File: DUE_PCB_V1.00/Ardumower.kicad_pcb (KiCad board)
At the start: 2 copper layers, 169.8 x 97 mm, 86 parts, among them J1 9V IN, J10 Sonar_R, J11 Sonar_C, J12 Sonar_L, J13 P_Right, J14 Buzzer, J15 Button, J16 US1, J17 US2, J18 US3, J19 P_Left, J2 I2C0_1, J20 Remote, J21 PCB_2, J22 Ser0, J23 Ser1, J24 Ser2, J25 5V IN, J26 Cutter1, J27 MotorR, J28 MotorL, J29 3.3V IN, J3 I2C0_2, J30 I2C1_2, J31 Ser3, J32 24V In, J33 ReserveD8, J34 ReserveD9, J35 ReserveD49, J36 ReserveA10, J37 RPM_Mow, J38 ODO_Left, J39 ODO_Right, J4 I2C1_1, J40 Motor_Right, J41 Motor_Left, J42 Cutter, J5 Bumper, J6 Drop_Left, J7 Drop_Right, J8 Tilt, J9 Rain, U1 MC33926, U2 MC33926

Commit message: First Route Test
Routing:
- net GND: track 0.00 -> 656.8 mm
- net +3V3: track 0.00 -> 336.2 mm
- net +5V: track 0.00 -> 323.6 mm, vias 0 -> 1
- net IOREV: track 0.00 -> 163.4 mm
- net pinBuzzer: track 0.00 -> 129.3 mm
- net pinChargeRelay: track 0.00 -> 128.2 mm
- net pinRemoteSwitch: track 0.00 -> 126.1 mm
- net pinButton: track 0.00 -> 125.1 mm
- net pinUserSwitch3: track 0.00 -> 121.3 mm
- net pinMotorMowSense: track 0.00 -> 117.9 mm, vias 0 -> 1
- net pinMotorLeftPWM: track 0.00 -> 116.1 mm
- net pinDropRight: track 0.00 -> 109.7 mm
- net pinChargeVoltage: track 0.00 -> 106.5 mm, vias 0 -> 1
- net pinMotorRightPWM: track 0.00 -> 104.5 mm
- net pinChargeCurrent: track 0.00 -> 102.8 mm, vias 0 -> 1
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
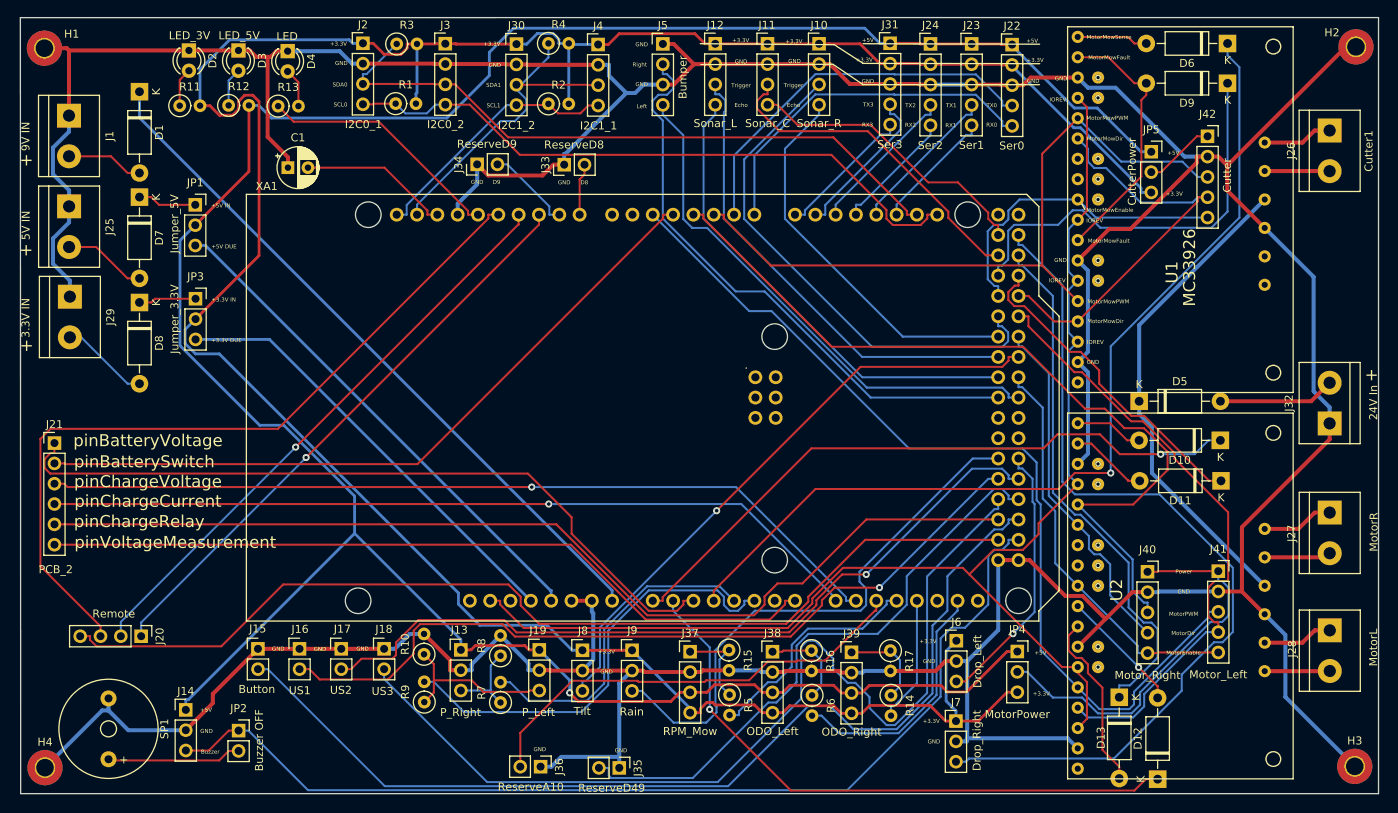
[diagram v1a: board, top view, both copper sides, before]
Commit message: Small changes in Line Traces
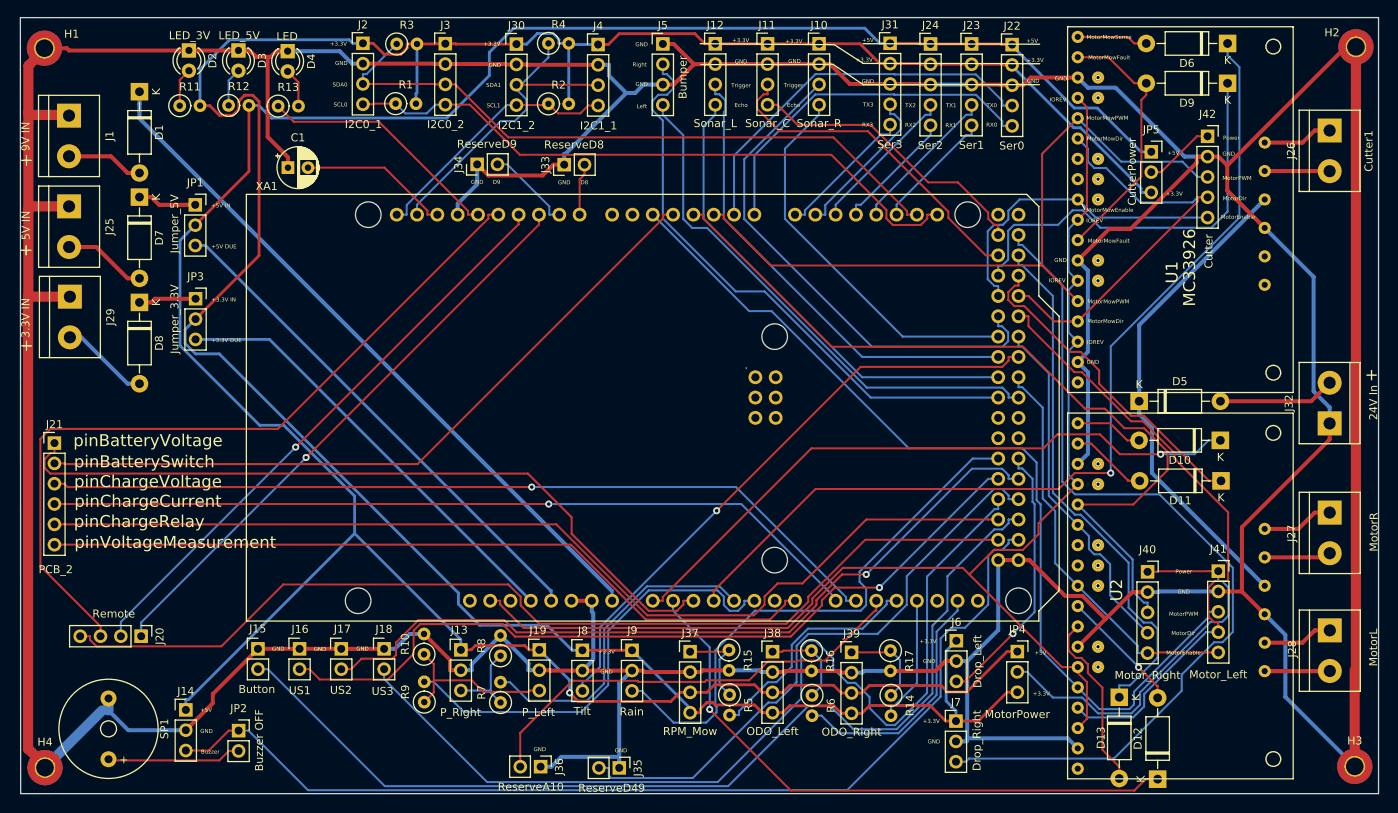
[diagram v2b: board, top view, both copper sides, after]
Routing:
- net GND: track 656.8 -> 822.6 mm

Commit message: Add Gerber Files
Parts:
- added REF**: WEEE-Logo_4.2x6mm_SilkScreen, Symbol:WEEE-Logo_4.2x6mm_SilkScreen, F.Cu at (84.9, 127.2)
- added REF**: ESD-Logo_8.9x8mm_SilkScreen, Symbol:ESD-Logo_8.9x8mm_SilkScreen, F.Cu at (75.8, 125.8)
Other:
- board text added: "Simple Mower Main PCB v1.01 by SD 05/2021 Attention only for Arduino DUE"

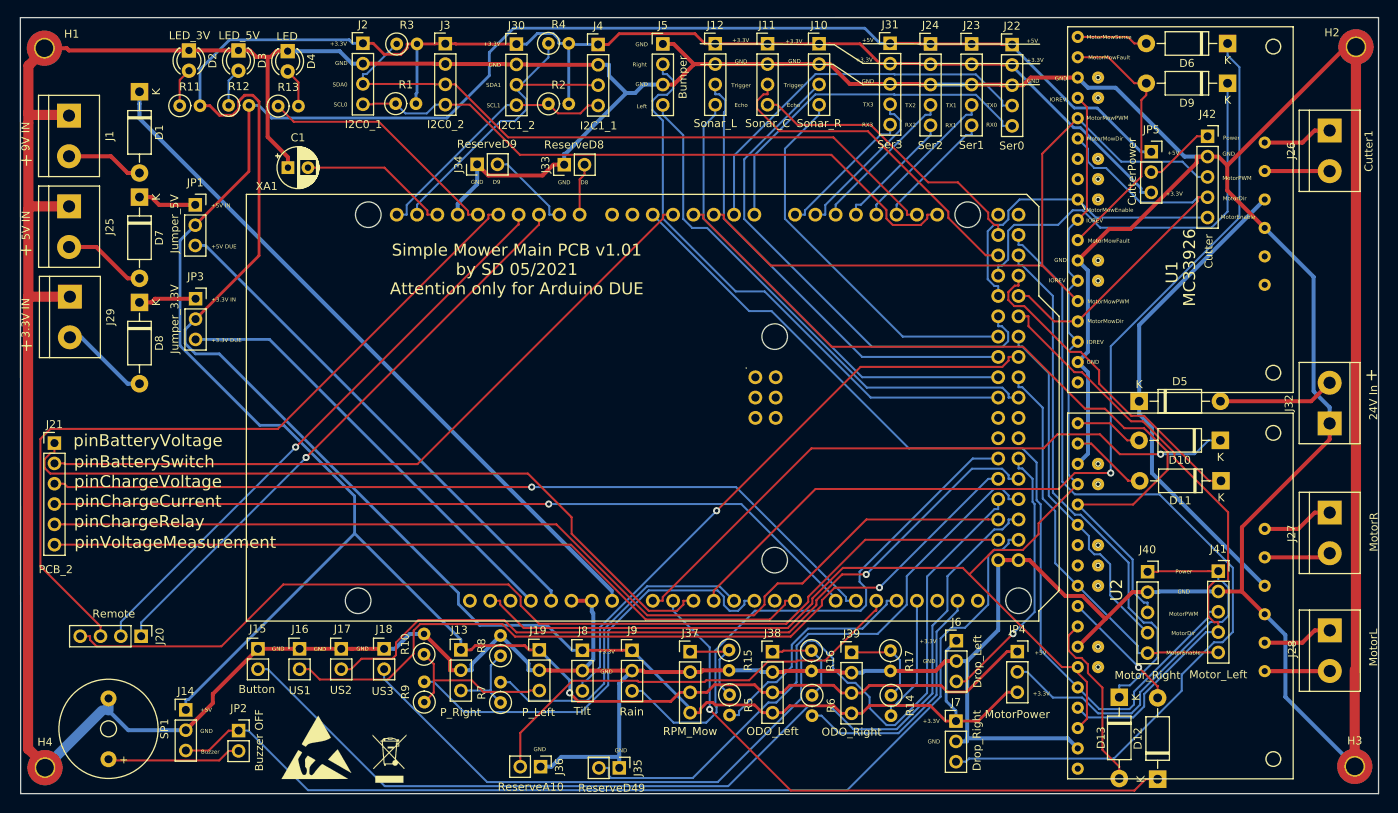
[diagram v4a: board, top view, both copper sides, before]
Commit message: Remove 24V from PCB
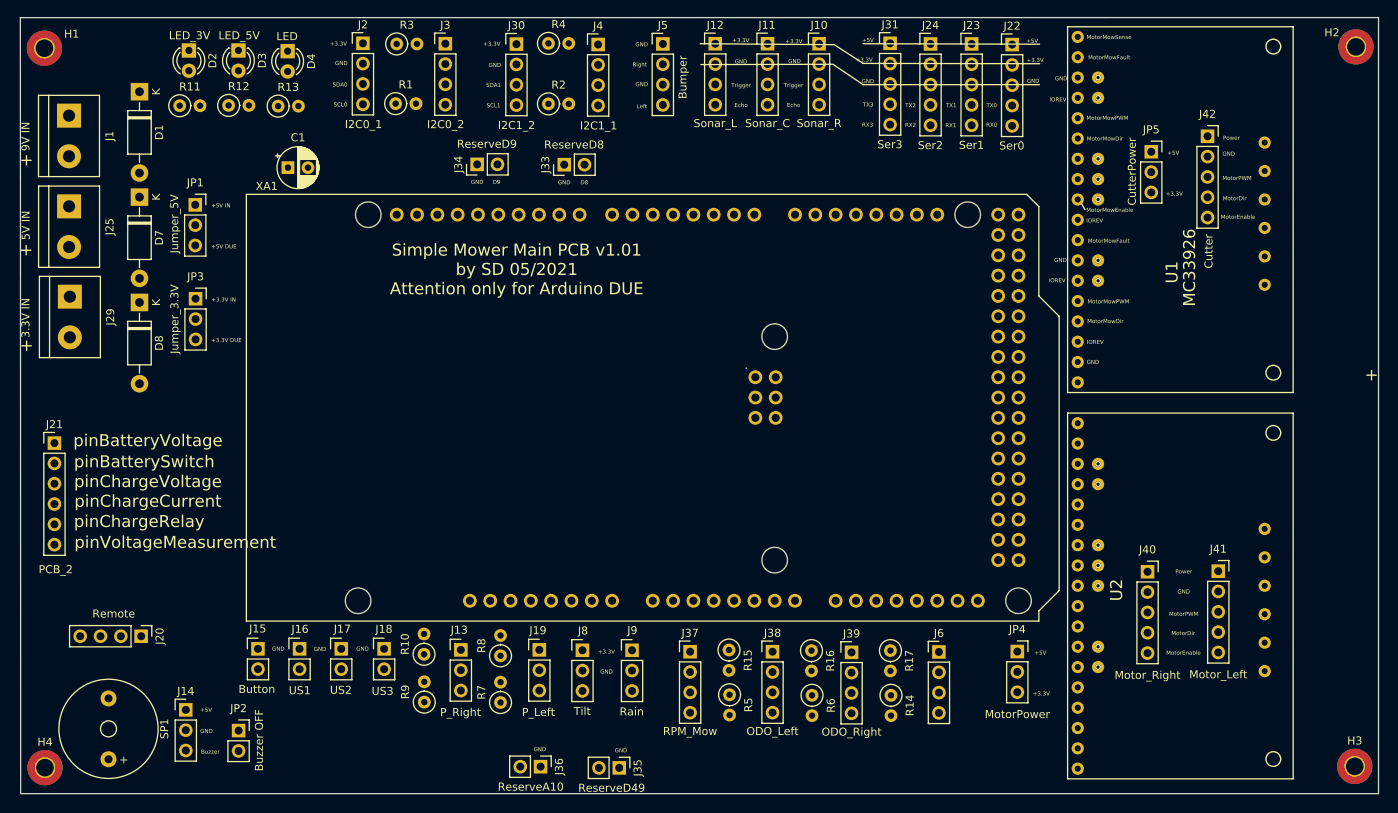
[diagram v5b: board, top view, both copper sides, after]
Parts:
- removed D10, D11, D12, D13, D5, D6, D9: 1N4728A, Diode_THT:D_DO-41_SOD81_P10.16mm_Horizontal
- removed J26: Cutter1, TerminalBlock:TerminalBlock_bornier-2_P5.08mm
- removed J27: MotorR, TerminalBlock:TerminalBlock_bornier-2_P5.08mm
- removed J28: MotorL, TerminalBlock:TerminalBlock_bornier-2_P5.08mm
- removed J32: 24V In, TerminalBlock:TerminalBlock_bornier-2_P5.08mm
- removed J7: Drop_Right, Connector_PinHeader_2.54mm:PinHeader_1x03_P2.54mm_Vertical
- removed REF**: WEEE-Logo_4.2x6mm_SilkScreen, Symbol:WEEE-Logo_4.2x6mm_SilkScreen
- removed REF**: ESD-Logo_8.9x8mm_SilkScreen, Symbol:ESD-Logo_8.9x8mm_SilkScreen
- J6: value Drop_Left -> Drop; footprint Connector_PinHeader_2.54mm:PinHeader_1x03_P2.54mm_Vertical -> Connector_PinHeader_2.54mm:PinHeader_1x04_P2.54mm_Vertical
- moved J6 2.59 mm to (153.6, 113.9)
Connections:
- J21 pad 6: pinVoltageMeasurement -> +3V3
- J6 pad 1: +3V3 -> GND
- J6 pad 2: GND -> pinDropLeft
- J6 pad 3: pinDropLeft -> GND
- U1 pad 17: Net-(D9-Pad2) -> pinMotorMowFault
- U1 pad 18: Net-(D6-Pad2) -> pinMotorMowSense
- U1 pad 21: GND -> (no net)
- U1 pad 22: +24V -> (no net)
- U1 pad 23: Net-(J26-Pad2) -> (no net)
- U1 pad 24: Net-(J26-Pad1) -> (no net)
- U1 pad 8: Net-(D9-Pad2) -> pinMotorMowFault
- U2 pad 17: Net-(D11-Pad2) -> pinMotorRightFault
- U2 pad 18: Net-(D10-Pad2) -> pinMotorRightSense
- U2 pad 19: Net-(J28-Pad2) -> (no net)
- U2 pad 20: Net-(J28-Pad1) -> (no net)
- U2 pad 21: GND -> (no net)
- U2 pad 22: +24V -> (no net)
- U2 pad 23: Net-(J27-Pad2) -> (no net)
- U2 pad 24: Net-(J27-Pad1) -> (no net)
- U2 pad 8: Net-(D13-Pad2) -> pinMotorLeftFault
- U2 pad 9: Net-(D12-Pad2) -> pinMotorLeftSense
- XA1 pad A7: pinVoltageMeasurement -> (no net)
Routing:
- net GND: track 822.6 -> 0.00 mm
- net +3V3: track 336.2 -> 0.00 mm
- net +5V: track 323.6 -> 0.00 mm, vias 1 -> 0
- net IOREV: track 163.4 -> 0.00 mm
- net pinBuzzer: track 129.3 -> 0.00 mm
- net pinChargeRelay: track 128.2 -> 0.00 mm
- net pinRemoteSwitch: track 126.1 -> 0.00 mm
- net pinButton: track 125.1 -> 0.00 mm
- net pinUserSwitch3: track 121.3 -> 0.00 mm
- net pinMotorMowSense: track 117.9 -> 0.00 mm, vias 1 -> 0
- net pinMotorLeftPWM: track 116.1 -> 0.00 mm
- net pinDropRight: track 109.7 -> 0.00 mm
- net pinChargeVoltage: track 106.5 -> 0.00 mm, vias 1 -> 0
- net pinMotorRightPWM: track 104.5 -> 0.00 mm
- net pinChargeCurrent: track 102.8 -> 0.00 mm, vias 1 -> 0
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
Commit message: Add 2 new Motor Connectors and Odo
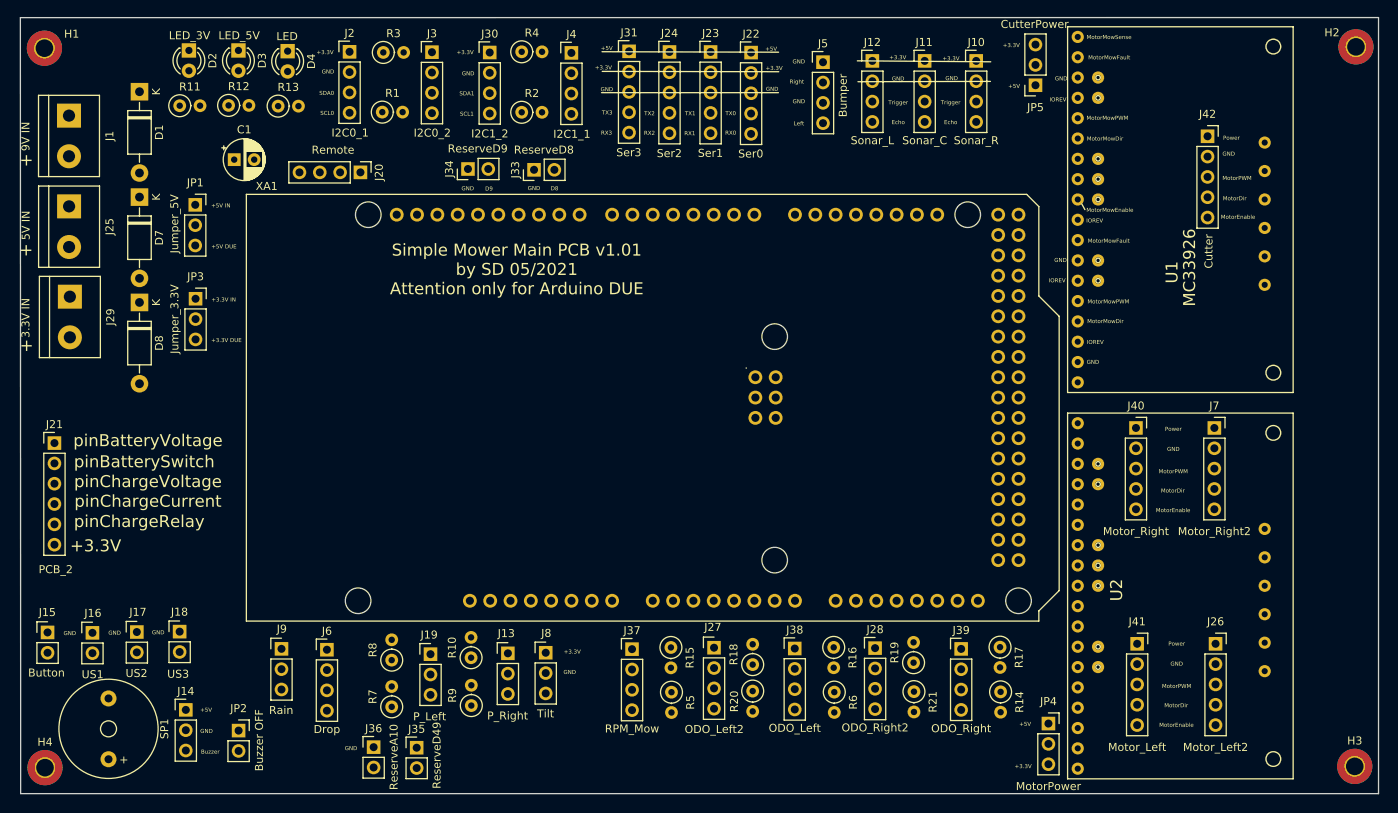
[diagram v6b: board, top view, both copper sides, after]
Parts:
- added J26: Motor_Left2, Connector_PinSocket_2.54mm:PinSocket_1x05_P2.54mm_Vertical, F.Cu at (188.2, 112.9)
- added J27: ODO_Left2, Connector_PinHeader_2.54mm:PinHeader_1x04_P2.54mm_Vertical, F.Cu at (125.5, 113.4)
- added J28: ODO_Right2, Connector_PinHeader_2.54mm:PinHeader_1x04_P2.54mm_Vertical, F.Cu at (145.6, 113.4)
- added J7: Motor_Right2, Connector_PinSocket_2.54mm:PinSocket_1x05_P2.54mm_Vertical, F.Cu at (188.1, 85.9)
- added R18: 1KO, Resistor_THT:R_Axial_DIN0207_L6.3mm_D2.5mm_P2.54mm_Vertical, F.Cu at (130.3, 115.5)
- added R19: 1KO, Resistor_THT:R_Axial_DIN0207_L6.3mm_D2.5mm_P2.54mm_Vertical, F.Cu at (150.4, 115.2)
- added R20: 1,5KO, Resistor_THT:R_Axial_DIN0207_L6.3mm_D2.5mm_P2.54mm_Vertical, F.Cu at (130.3, 118.8)
- added R21: 1,5KO, Resistor_THT:R_Axial_DIN0207_L6.3mm_D2.5mm_P2.54mm_Vertical, F.Cu at (150.5, 118.9)
- moved J6 76.5 mm to (77.1, 113.6)
- moved J20 64.1 mm to (81.3, 54.0)
- moved J9 43.8 mm to (71.4, 113.5)
- moved J22 32.6 mm to (130.1, 39.0)
- moved J23 32.6 mm to (125.1, 38.9)
- moved J31 32.6 mm to (114.9, 38.8)
- moved J24 32.6 mm to (119.9, 38.9)
- moved J15 26.4 mm to (42.2, 111.5)
- moved J16 26.0 mm to (47.8, 111.5)
- moved J18 25.7 mm to (58.7, 111.4)
- moved J17 25.6 mm to (53.4, 111.4)
- moved J35 25.4 mm to (88.3, 125.9), turned to 0 degrees
- moved J36 21.0 mm to (83.0, 125.8), turned to 0 degrees
- moved J5 20.1 mm to (139.1, 40.2)
- moved J10 19.8 mm to (158.3, 40.0)
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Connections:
- XA1 pad CANT: (no net) -> pinOdometryRight2
- XA1 pad DAC1: (no net) -> pinOdometryLeft2
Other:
- board text removed: "pinVoltageMeasurement"

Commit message: Changes
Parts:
- removed D3: LED_5V, LED_THT:LED_D3.0mm
- removed D4: LED, LED_THT:LED_D3.0mm
- removed J35: ReserveD49, Connector_PinHeader_2.54mm:PinHeader_1x02_P2.54mm_Vertical
- removed J37: RPM_Mow, Connector_PinHeader_2.54mm:PinHeader_1x04_P2.54mm_Vertical
- removed R12: 220, Resistor_THT:R_Axial_DIN0207_L6.3mm_D2.5mm_P2.54mm_Vertical
- removed R13: 100, Resistor_THT:R_Axial_DIN0207_L6.3mm_D2.5mm_P2.54mm_Vertical
- removed R15: 1,5KO, Resistor_THT:R_Axial_DIN0207_L6.3mm_D2.5mm_P2.54mm_Vertical
- removed R5: 1KO, Resistor_THT:R_Axial_DIN0207_L6.3mm_D2.5mm_P2.54mm_Vertical
- added J32: ReserveD13, Connector_PinHeader_2.54mm:PinHeader_1x02_P2.54mm_Vertical, F.Cu at (86.2, 53.8)
- J40: value Motor_Right -> Motor_Right1
- J41: value Motor_Left -> Motor_Left1
- moved J36 32.2 mm to (113.1, 114.3)
- moved J20 20.4 mm to (68.5, 38.0), turned to 0 degrees
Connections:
- J26 pad 3: (no net) -> pinMotorLeft2PWM
- J26 pad 4: (no net) -> pinMotorLeft2Dir
- J26 pad 5: pinMotorEnable -> pinMotorLeft2Enable
- J40 pad 1: Net-(J40-Pad1) -> Net-(J26-Pad1)
- J41 pad 1: Net-(J40-Pad1) -> Net-(J26-Pad1)
- J41 pad 5: pinMotorEnable -> pinMotorLeftEnable
- J7 pad 3: (no net) -> pinMotorRight2PWM
- J7 pad 4: (no net) -> pinMotorRight2Dir
- J7 pad 5: pinMotorEnable -> pinMotorRight2Enable
- JP4 pad 2: Net-(J40-Pad1) -> Net-(J26-Pad1)
- R11 pad 2: +3V3 -> DUE_3.3V
- U1 pad 9: IOREV -> pinMotorMow1Sense
- XA1 pad A11: pinMotorMowRpm -> (no net)
- XA1 pad A6: (no net) -> pinMotorMow1Sense
- XA1 pad D13: pinLED -> pinReserveD13
- XA1 pad D40: (no net) -> pinMotorLeft2Dir
- XA1 pad D41: (no net) -> pinMotorRight2Dir
- XA1 pad D42: (no net) -> pinMotorLeft2Enable
- XA1 pad D43: (no net) -> pinMotorRight2Enable
- XA1 pad D49: pinReserveD49 -> pinMotorLeftEnable
- XA1 pad D6: (no net) -> pinMotorLeft2PWM
- XA1 pad D7: (no net) -> pinMotorRight2PWM
